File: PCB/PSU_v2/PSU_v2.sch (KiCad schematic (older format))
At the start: 19 parts, among them J1 CONN_01X05, Q1 MPSA55, Q2 IRF630, U1 MC34063

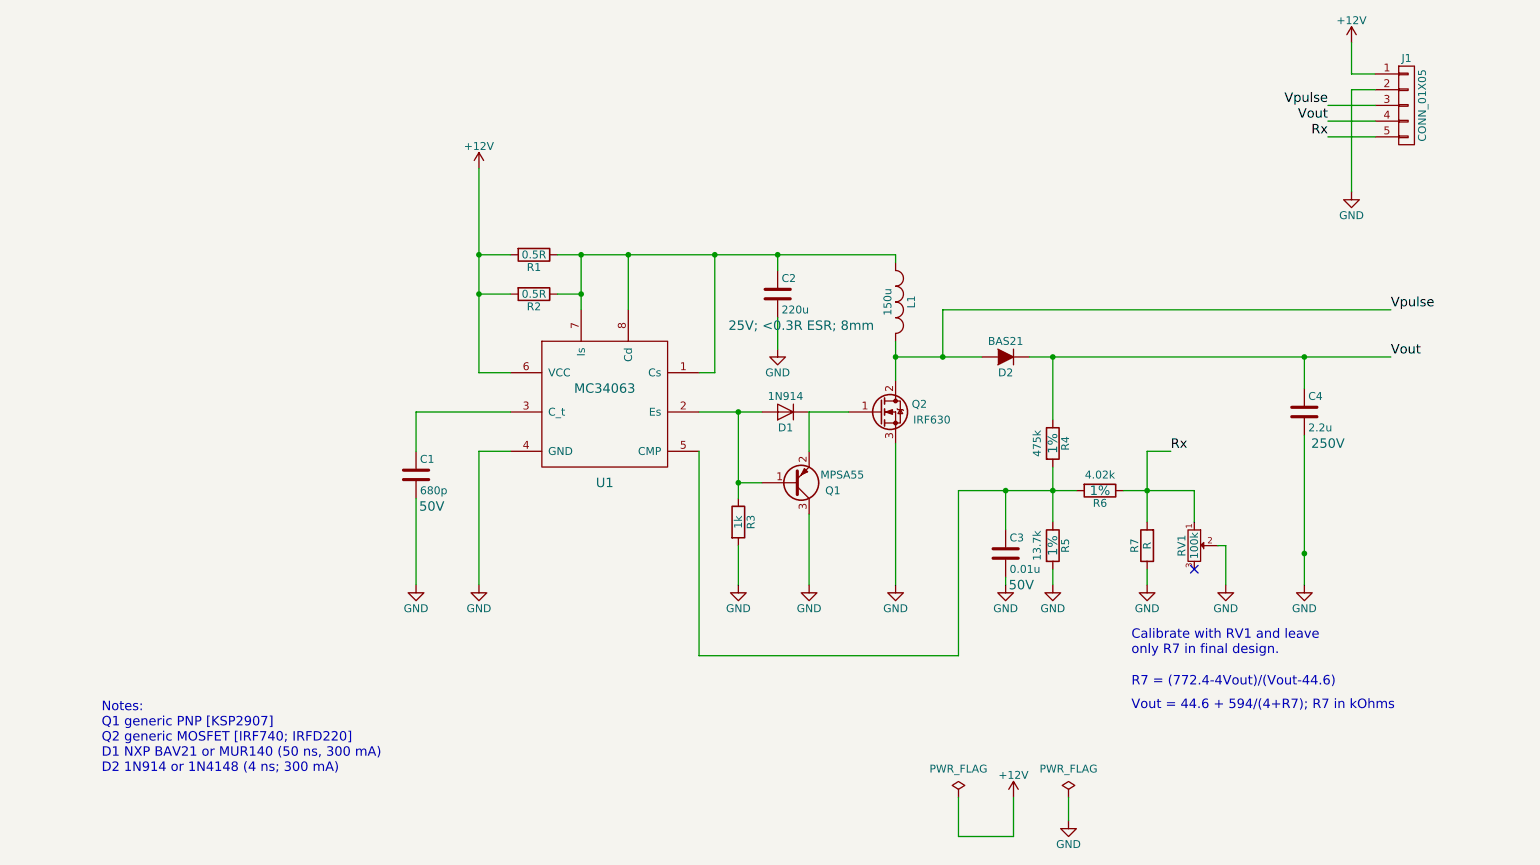
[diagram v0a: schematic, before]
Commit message: Corrected MOSFET footprint, added test points, made resistor values sane. Also some comments on over-current protection
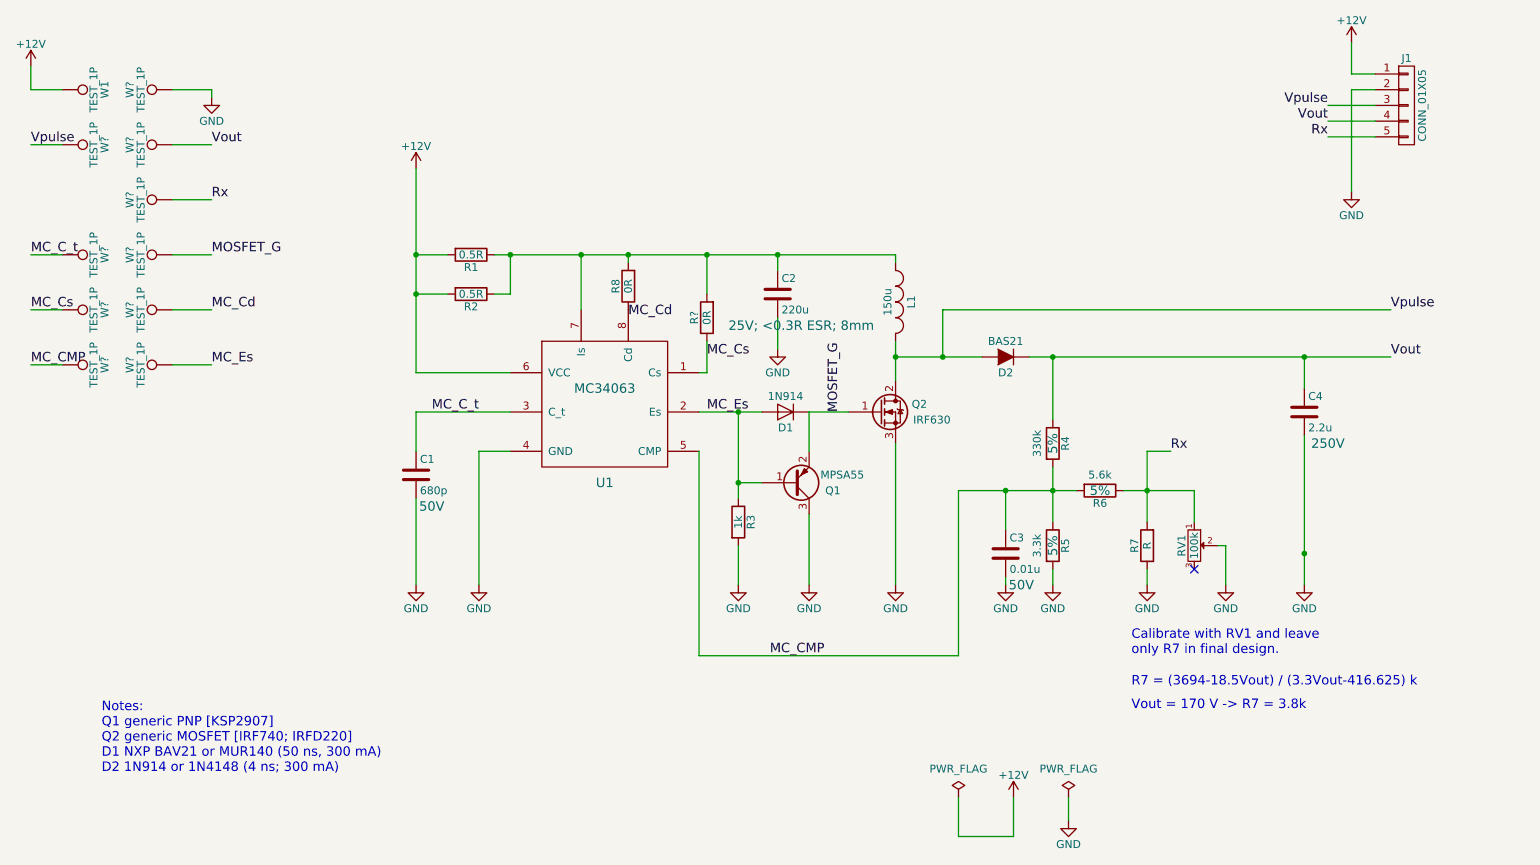
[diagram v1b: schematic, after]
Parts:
- added R8, R?: 0R, Resistors_SMD:R_0805_HandSoldering, symbol R
- added W1, W? (x10): TEST_1P, symbol TEST_1P
- Q2: footprint TO_SOT_Packages_SMD:TO-252-2Lead -> nixie_fp:TO-263-2Lead
- R4: value 475k -> 330k; Field4 1% -> 5%
- R5: value 13.7k -> 3.3k; Field4 1% -> 5%
- R6: value 4.02k -> 5.6k; Field4 1% -> 5%
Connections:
- net +12V: now also W1.1
- net GND: now also W?.1
- net Rx: now also W?.1
- net Vout: now also W?.1
- net Vpulse: now also W?.1
- net at C2.1, L1.1, R1.1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: now also R8.2, R?.2; no longer U1.1 (Cs), U1.8 (Cd)
- net MC_Es: now reaches D1.2 (A), Q1.1 (B), R3.1, U1.2 (Es)
- net MC_Es: now also W?.1
- net MC_C_t: now reaches C1.1, U1.3 (C_t)
- net MC_C_t: now also W?.1
- net MC_CMP: now reaches C3.1, R4.2, R5.1, R6.2, U1.5 (CMP)
- net MC_CMP: now also W?.1
- net MOSFET_G: now reaches D1.1 (K), Q1.2 (E), Q2.1 (G)
- net MOSFET_G: now also W?.1
- new net: R8.1, U1.8 (Cd)
- new net MC_Cd: W?.1
- new net MC_Cs: R?.1, U1.1 (Cs), W?.1
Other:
- note added: "R7 = (3694-18.5Vout) / (3.3Vout-416.625) k"
- note added: "Vout = 170 V -> R7 = 3.8k"
- note removed: "R7 = (772.4-4Vout)/(Vout-44.6)"
- note removed: "Vout = 44.6 + 594/(4+R7); R7 in kOhms"
- moved on the sheet: R1, R2

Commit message: PCB for HV PSU v2 prototype
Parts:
- removed W? (x2): TEST_1P, symbol TEST_1P
- R4, R5: footprint Resistors_SMD:R_0603_HandSoldering -> Resistors_SMD:R_0805_HandSoldering
- RV1: symbol POT -> POT-RESCUE-PSU_v2
- W1: footprint (none) -> Measurement_Points:Measurement_Point_Round-SMD-Pad_Small
- W10, W11, W3, W4, W5, W7, W8, W9: renamed from W?; footprint (none) -> Measurement_Points:Measurement_Point_Round-SMD-Pad_Small
- gave numbers to parts that had none: 1
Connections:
- net +12V: now also J1.3 (P3); no longer J1.1 (P1)
- net GND: now also J1.1 (P1); no longer J1.2 (P2)
- net MC_Cd: now also R8.1, U1.8 (Cd)
- net Rx: now also RV1.3; no longer RV1.1
- net Vpulse: now also J1.2 (P2); no longer J1.3 (P3)
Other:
- moved on the sheet: R8
